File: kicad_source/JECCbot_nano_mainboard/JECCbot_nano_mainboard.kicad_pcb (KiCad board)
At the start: 2 copper layers, 80 x 80 mm, 34 parts, among them CN1 ADAFRUIT_FEATHER, CN2 CONN_01X02, CN3 CONN_01X02, SW1 SWITCH_INV, U1 VL53L0X_breakout, U2 VL53L0X_breakout, U3 VL53L0X_breakout, U4 VL53L0X_breakout, U5 VL53L0X_breakout, U6 TCA9534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

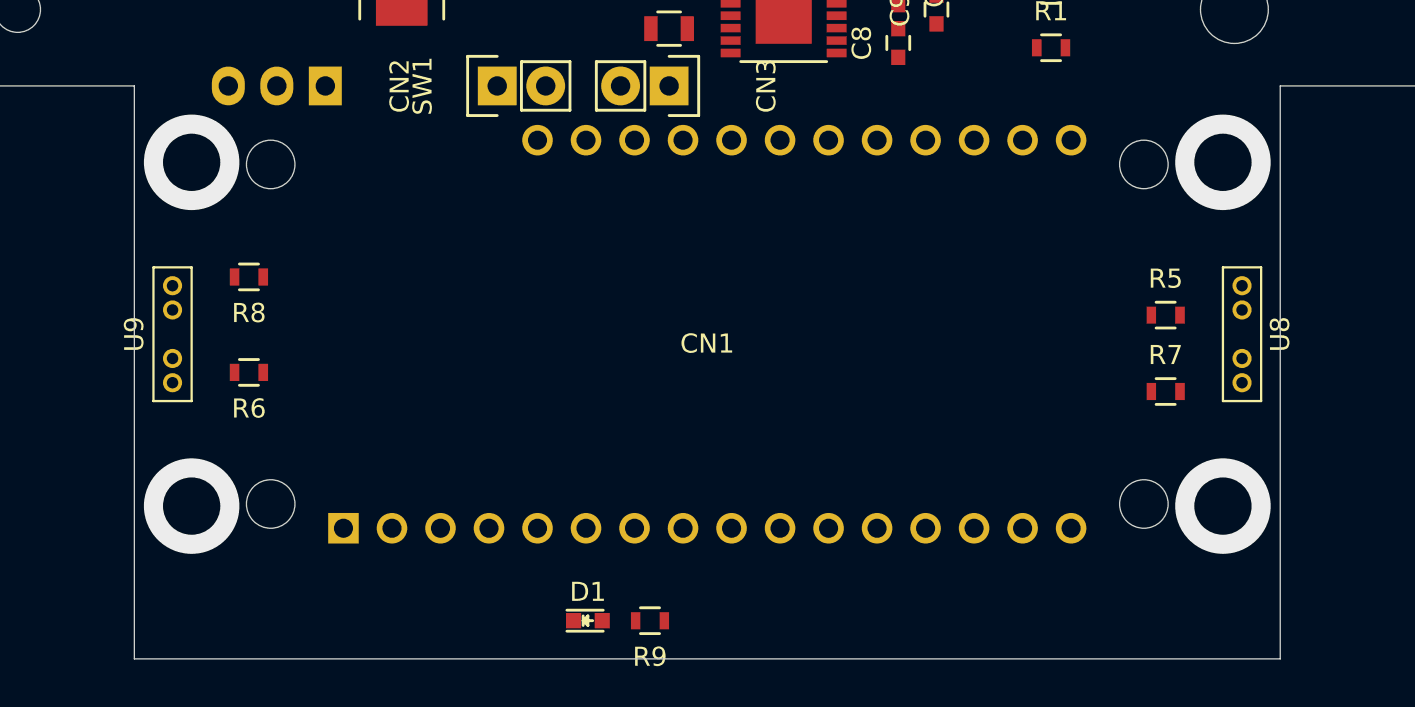
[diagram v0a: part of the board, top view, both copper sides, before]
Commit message: moved motors 2 mm backwards to make space for bigger wheels and generated step file
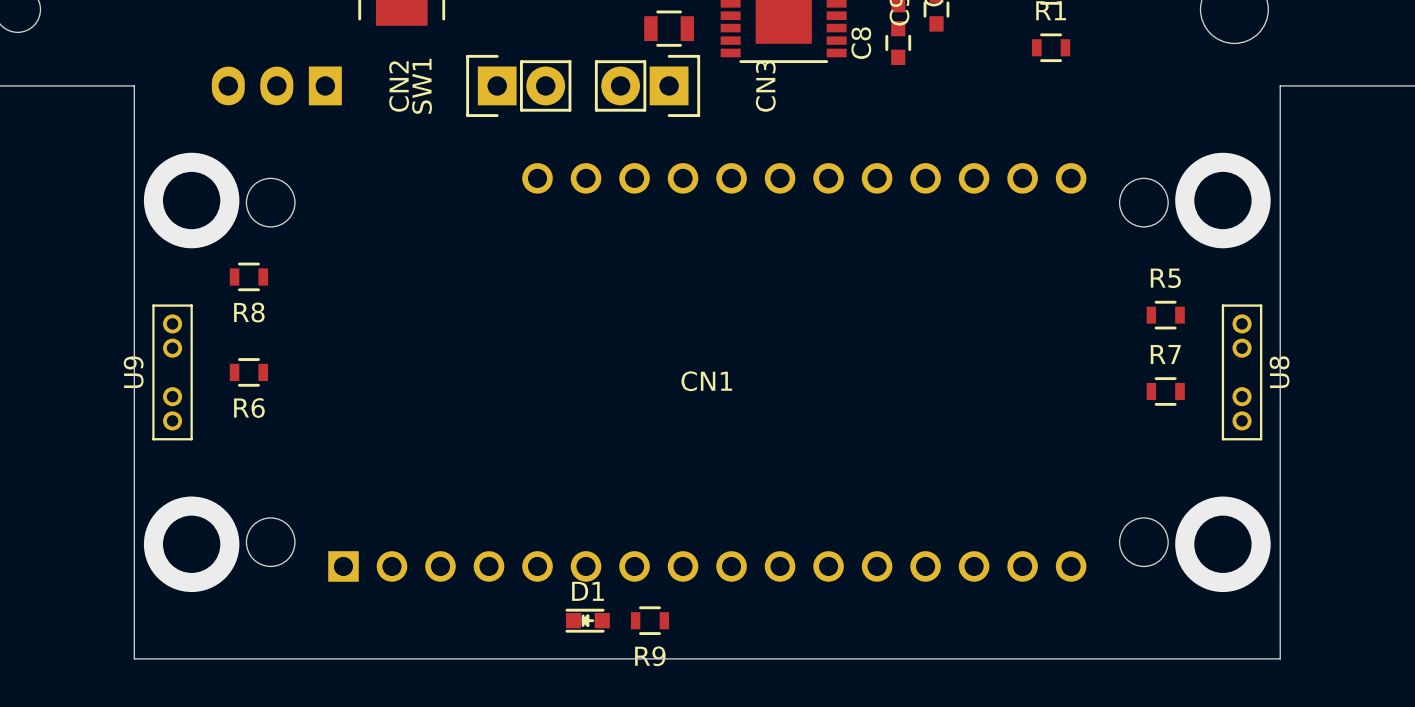
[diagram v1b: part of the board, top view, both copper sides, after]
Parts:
- moved CN1 2.00 mm to (110.0, 135.0)
- moved U8 2.00 mm to (138.0, 135.0)
- moved U9 2.00 mm to (82.0, 135.0)
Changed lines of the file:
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@@
   )
   (module MODULE_compute:ADAFRUIT_FEATHER_HOLES (layer F.Cu)
-    (at 110 133)
+    (at 110 135)
     (fp_text reference CN1 (at 0 0.5) (layer F.SilkS)
       (effects (font (size 1 1) (thickness 0.15)))
@@
   )
   (module IC_sensor:TCRT1000 (layer F.Cu)
-    (at 138 133 90)
+    (at 138 135 90)
     (descr "Reflective Optical Sensor with Transistor Output")
     (tags "Reflective Optical Sensor with Transistor Output")
@@
   )
   (module IC_sensor:TCRT1000 (layer F.Cu)
-    (at 82 133 270)
+    (at 82 135 270)
     (descr "Reflective Optical Sensor with Transistor Output")
     (tags "Reflective Optical Sensor with Transistor Output")
@@
   (gr_line (start 80 120) (end 80 150) (layer Edge.Cuts) (width 0.05))
   (gr_line (start 70 120) (end 80 120) (layer Edge.Cuts) (width 0.05))
-  (via (at 83 124) (size 5) (drill 3) (layers F.Cu B.Cu) (net 0))
-  (via (at 83 142) (size 5) (drill 3) (layers F.Cu B.Cu) (net 0))
-  (via (at 137 142) (size 5) (drill 3) (layers F.Cu B.Cu) (net 0))
-  (via (at 137 124) (size 5) (drill 3) (layers F.Cu B.Cu) (net 0))
+  (via (at 83 126) (size 5) (drill 3) (layers F.Cu B.Cu) (net 0))
+  (via (at 83 144) (size 5) (drill 3) (layers F.Cu B.Cu) (net 0))
+  (via (at 137 144) (size 5) (drill 3) (layers F.Cu B.Cu) (net 0))
+  (via (at 137 126) (size 5) (drill 3) (layers F.Cu B.Cu) (net 0))
 )
